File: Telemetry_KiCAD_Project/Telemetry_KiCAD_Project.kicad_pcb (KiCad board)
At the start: 4 copper layers, 80 x 87.3 mm, 67 parts, among them J1 50Ω SMA Connector, J2 DB37_Male, J3 10118192-0001LF, U2 Si4463, U3 ADL5521, U4 Si4463, U5 STM32L562VET, U6 LM317T, U7 USBLC6-2SC6, Y1 30MHz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

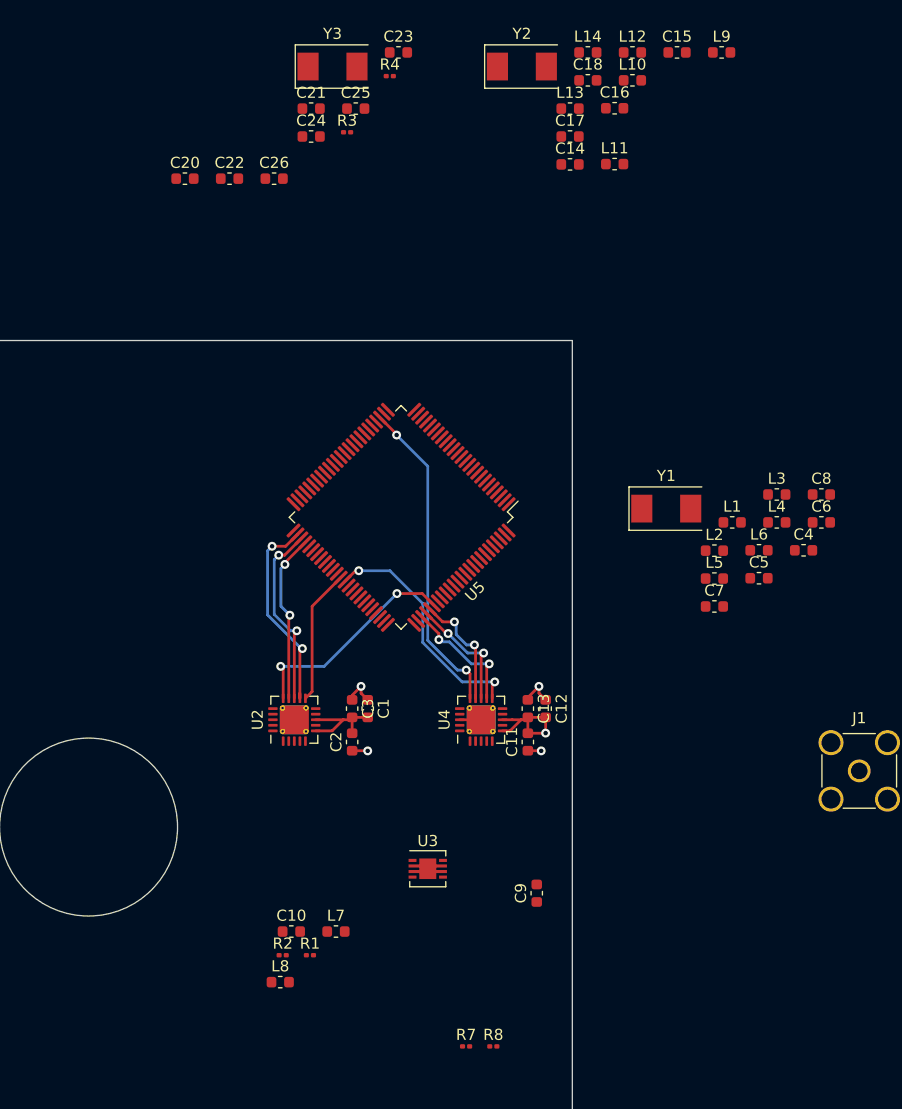
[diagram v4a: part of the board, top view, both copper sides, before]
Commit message: Added TX/RX matching network passives to PCB
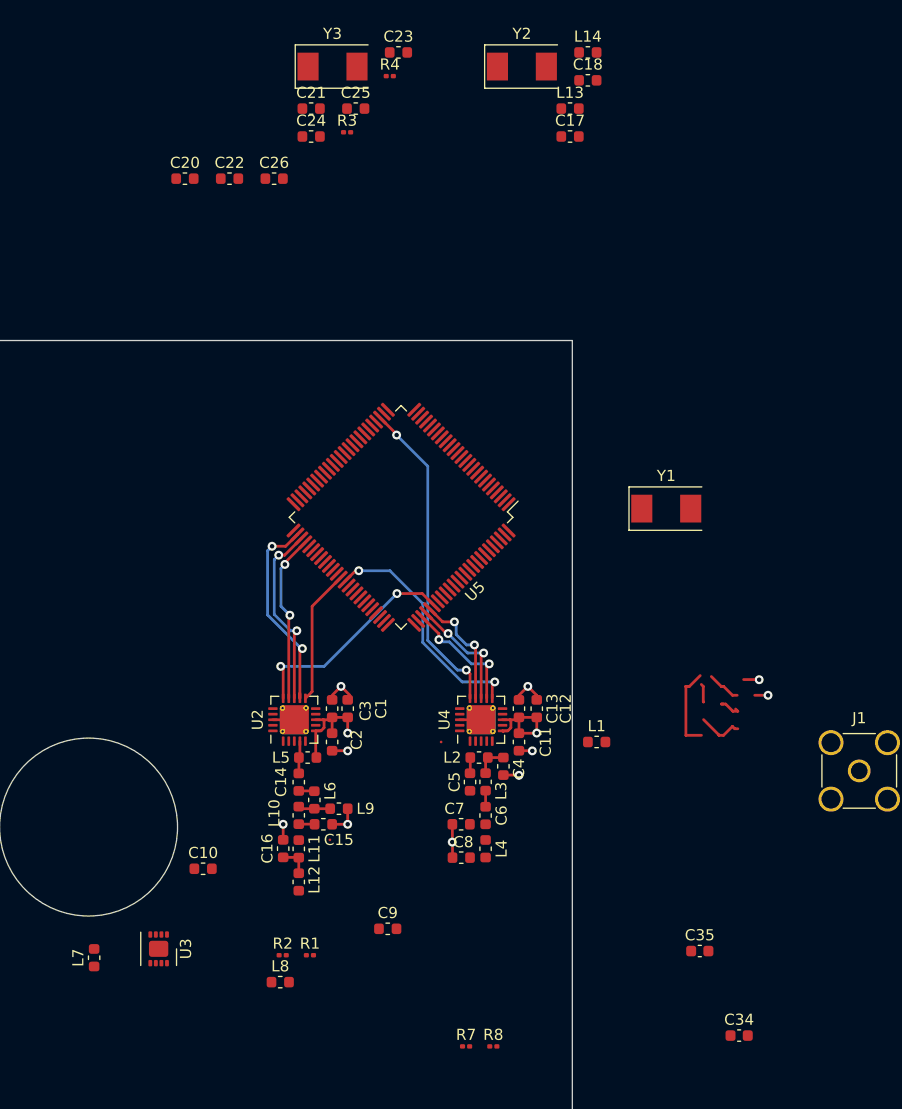
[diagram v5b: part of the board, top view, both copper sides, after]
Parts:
- added C34: C_Small, Capacitor_SMD:C_0603_1608Metric, F.Cu at (201.8, 117.8)
- added C35: C_Small, Capacitor_SMD:C_0603_1608Metric, F.Cu at (198.3, 110.2)
- C14: value C_Small -> 4.7pF
- C15, C16: value C_Small -> 3.3pF
- C4: value C_Small -> 3pF
- C5: value C_Small -> 1pF
- C6: value C_Small -> DC_Blocking
- C7, C8: value C_Small -> 4.3pF
- L1, L5: value L_Small -> 100nH
- L10, L12: value L_Small -> 11nH
- L11, L3: value L_Small -> 22nH
- L2: value L_Small -> 18nH
- L4: value L_Small -> 8.2nH
- L6: value L_Small -> 3.3nH
- L9: value L_Small -> 6.2nH
- U3: footprint Package_CSP:Analog_LFCSP-8-1EP_3x3mm_P0.5mm_EP1.53x1.85mm -> Package_CSP:LFCSP-8-1EP_3x3mm_P0.5mm_EP1.45x1.74mm
- moved L12 80.4 mm to (162.2, 104.0), turned to 270 degrees
- moved C15 76.3 mm to (164.4, 98.8)
- moved L9 76.2 mm to (165.8, 97.4)
- moved C16 72.9 mm to (160.8, 101.0), turned to 90 degrees
- moved L10 72.6 mm to (162.2, 98.0), turned to 270 degrees
- moved L11 67.8 mm to (162.2, 101.0), turned to 270 degrees
- moved C14 60.7 mm to (162.2, 95.0), turned to 270 degrees
- moved C8 46.0 mm to (176.8, 101.8), turned to 180 degrees
- moved L6 45.9 mm to (163.6, 96.6), turned to 270 degrees
- moved C6 40.1 mm to (179.0, 98.0), turned to 270 degrees
- moved L5 40.0 mm to (163.0, 92.8)
- moved L4 39.3 mm to (179.0, 101.0), turned to 270 degrees
- moved L3 36.8 mm to (179.0, 95.0), turned to 270 degrees
- moved C4 33.3 mm to (180.6, 93.6), turned to 90 degrees
- moved C5 31.8 mm to (177.6, 95.0), turned to 270 degrees
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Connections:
- C15 pad 2: Net-(C15-Pad2) -> GND
- C16 pad 1: GND -> Net-(C16-Pad1)
- C16 pad 2: Net-(C15-Pad1) -> GND
- C18 pad 2: /RX_Si4463/RF_Out -> Net-(C18-Pad2)
- C4 pad 1: Net-(C4-Pad1) -> GND
- C6 pad 1: GND -> Net-(C5-Pad2)
- C6 pad 2: Net-(C5-Pad1) -> Net-(C6-Pad2)
- C7 pad 1: GND -> Net-(C6-Pad2)
- C7 pad 2: Net-(C7-Pad2) -> GND
- C8 pad 1: GND -> /RX_Si4463/RF_Out
- C8 pad 2: /ADL_Amplifier/RF_In -> GND
- L1 pad 1: +3V3 -> Net-(L1-Pad1)
- L1 pad 2: Net-(C4-Pad2) -> +3V3
- L10 pad 2: Net-(C15-Pad2) -> Net-(C15-Pad1)
- L11 pad 1: Net-(C14-Pad1) -> Net-(C15-Pad1)
- L11 pad 2: Net-(C15-Pad1) -> Net-(C16-Pad1)
- L12 pad 1: Net-(L10-Pad1) -> Net-(C16-Pad1)
- L12 pad 2: Net-(C15-Pad1) -> /ADL_Amplifier/RF_In
- L14 pad 2: /RX_Si4463/RF_Out -> Net-(C18-Pad2)
- L2 pad 1: Net-(L2-Pad1) -> Net-(C5-Pad1)
- L2 pad 2: Net-(C5-Pad2) -> Net-(C4-Pad2)
- L3 pad 1: Net-(C4-Pad1) -> Net-(C4-Pad2)
- L3 pad 2: Net-(C5-Pad1) -> Net-(C5-Pad2)
- L4 pad 1: Net-(L2-Pad1) -> Net-(C6-Pad2)
- L4 pad 2: Net-(C5-Pad1) -> /RX_Si4463/RF_Out
- L5 pad 1: Net-(C5-Pad1) -> Net-(C14-Pad1)
- L5 pad 2: Net-(C7-Pad2) -> +3V3
- L6 pad 1: Net-(C7-Pad2) -> Net-(C14-Pad2)
- L6 pad 2: /ADL_Amplifier/RF_In -> Net-(L10-Pad1)
- L9 pad 1: +3V3 -> Net-(L10-Pad1)
- L9 pad 2: Net-(C14-Pad2) -> GND
- U2 pad 2: Net-(L2-Pad1) -> Net-(U2-Pad2)
- U2 pad 3: Net-(C5-Pad2) -> Net-(U2-Pad3)
- U2 pad 4: Net-(C4-Pad2) -> Net-(C14-Pad1)
- U4 pad 2: Net-(L10-Pad1) -> Net-(C5-Pad1)
- U4 pad 3: Net-(C15-Pad2) -> Net-(C4-Pad2)
- U4 pad 4: Net-(C14-Pad2) -> Net-(L1-Pad1)
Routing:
- net GND: track 12.8 -> 24.0 mm, vias 5 -> 10
- net Net-(C4-Pad2): track 0.00 -> 9.80 mm
- net Net-(C6-Pad2): track 0.00 -> 7.51 mm
- net /RX_Si4463/RF_Out: track 0.00 -> 4.12 mm
- net Net-(C14-Pad1): track 0.00 -> 2.94 mm
- net Net-(L10-Pad1): track 0.00 -> 2.90 mm
- net Net-(C16-Pad1): track 0.00 -> 2.81 mm
- net +3V3: track 21.4 -> 19.2 mm, vias 1 -> 2
- net Net-(C5-Pad2): track 0.00 -> 1.45 mm
- net Net-(C15-Pad1): track 0.00 -> 1.45 mm
- net Net-(C5-Pad1): track 0.00 -> 1.42 mm
- net Net-(C14-Pad2): track 0.00 -> 1.41 mm
- net Net-(L1-Pad1): track 0.00 -> 1.20 mm, vias 0 -> 1

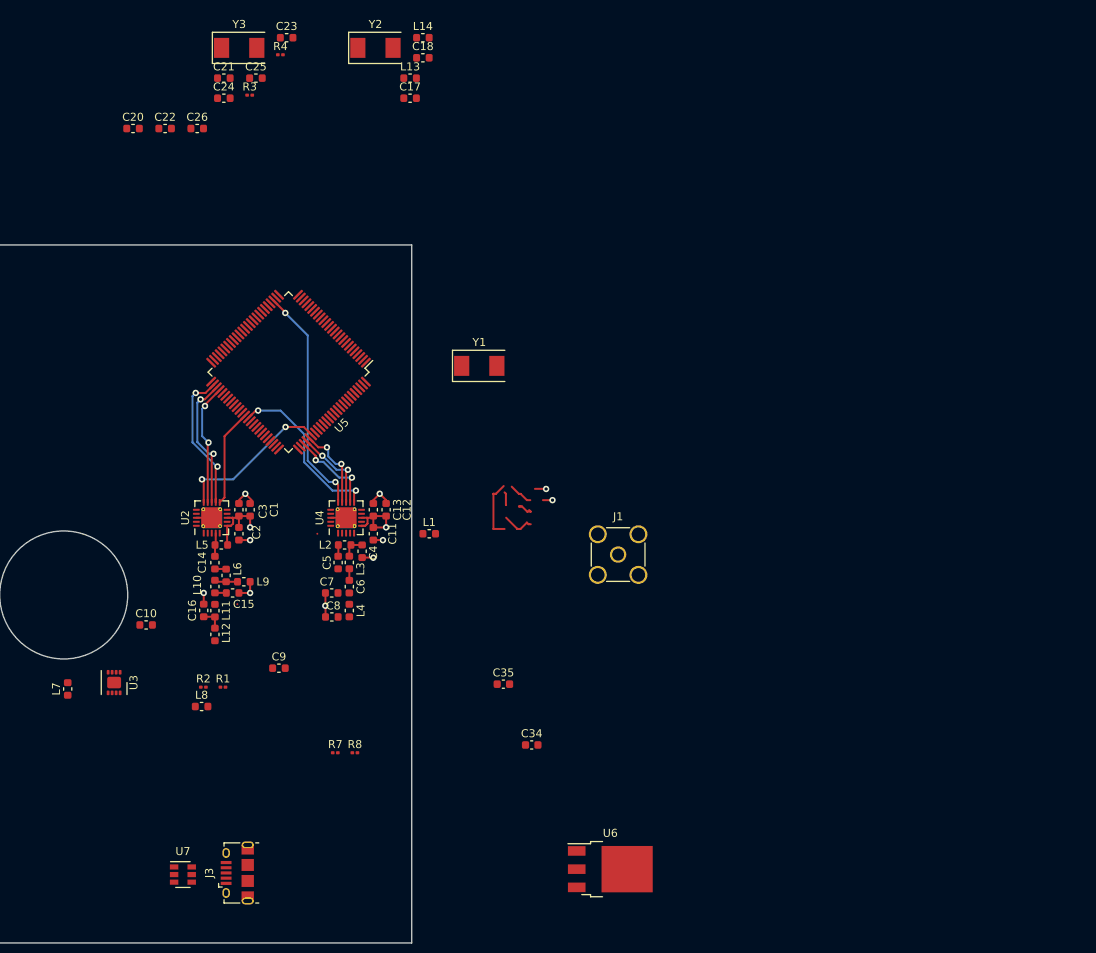
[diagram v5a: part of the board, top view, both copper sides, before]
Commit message: Added RSD Duplexer Footprint, rearranged RF matching networks
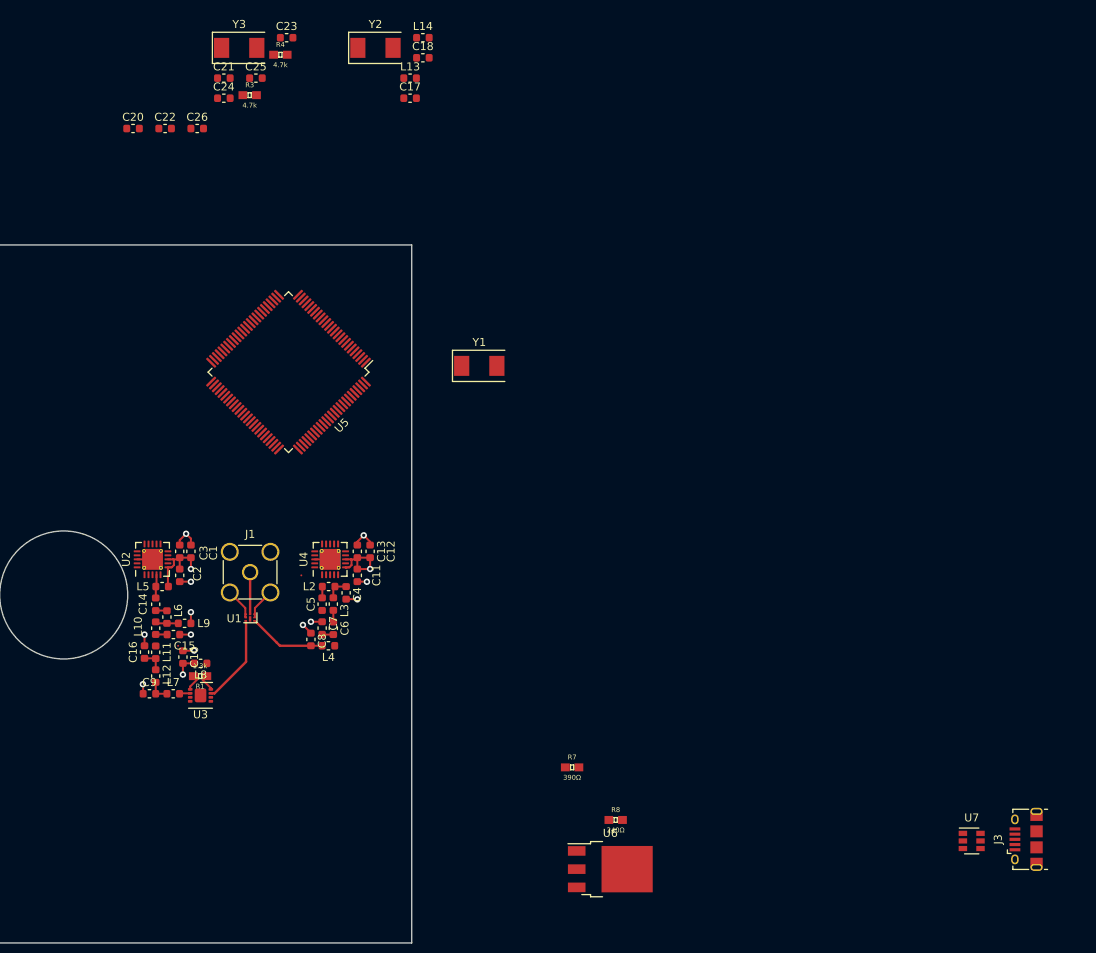
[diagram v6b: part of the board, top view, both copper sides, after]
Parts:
- removed C34, C35: C_Small, Capacitor_SMD:C_0603_1608Metric
- removed L1: 100nH, Inductor_SMD:L_0603_1608Metric
- removed R2: R_Small, Resistor_SMD:R_0201_0603Metric
- added U1: RSD-897.500-942.500-1612-TR, RDT_Custom_Footprints:RSD-897.500-942.500-1612-TR, F.Cu at (167.4, 102.5)
- L7: value L_Small -> 8.2nH
- R1, R3, R4, R7, R8: footprint Resistor_SMD:R_0201_0603Metric -> Resistors:0603
- moved J3 98.7 mm to (263.6, 129.6)
- moved U7 98.7 mm to (256.8, 129.8)
- moved J1 46.1 mm to (166.6, 96.2)
- moved R8 33.7 mm to (212.3, 127.2)
- moved R7 29.7 mm to (206.8, 120.6)
- moved C9 16.5 mm to (154.0, 111.4)
- moved L7 13.2 mm to (157.0, 111.4), turned to 0 degrees
- moved U3 10.9 mm to (160.4, 111.6), turned to 0 degrees
- moved C15 9.04 mm to (157.0, 104.0)
- moved C16 9.04 mm to (153.4, 106.2)
- moved L5 9.04 mm to (155.6, 98.0)
- moved L6 9.04 mm to (156.2, 101.8)
- moved C1 9.04 mm to (159.2, 93.6)
- moved L9 9.04 mm to (158.4, 102.6)
- moved U2 9.04 mm to (154.4, 94.6)
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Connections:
- C10 pad 2: Net-(C10-Pad2) -> +5V
- L8 pad 2: Net-(C10-Pad2) -> +5V
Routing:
- net /~RX_SEL: track 29.1 -> 0.00 mm, vias 2 -> 0
- net /~RX_IRQ: track 21.7 -> 0.00 mm, vias 2 -> 0
- net /~TX_SEL: track 19.9 -> 0.00 mm, vias 2 -> 0
- net /TX_SCL: track 18.5 -> 0.02 mm, vias 2 -> 0
- net /TX_SDO: track 17.0 -> 0.00 mm, vias 2 -> 0
- net /TX_SDI: track 15.3 -> 0.00 mm, vias 2 -> 0
- net /~TX_IRQ: track 12.2 -> 0.00 mm
- net /RX_SCL: track 11.3 -> 0.00 mm, vias 2 -> 0
- net /ADL_Amplifier/RF_Out: track 0.00 -> 10.9 mm
- net /RX_SDO: track 10.8 -> 0.00 mm, vias 2 -> 0
- net /RX_SDI: track 10.7 -> 0.00 mm, vias 2 -> 0
- net GND: track 24.0 -> 34.1 mm, vias 10 -> 13
- net Net-(C4-Pad2): track 9.80 -> 2.88 mm
- net Net-(C6-Pad2): track 7.51 -> 1.41 mm
- net /RX_Si4463/RF_Out: track 4.12 -> 9.52 mm
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
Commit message: PCB Layout Progress
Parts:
- removed C17, C18: C_Small, Capacitor_SMD:C_0603_1608Metric
- removed L13, L14: L_Small, Inductor_SMD:L_0603_1608Metric
- moved C19 183.4 mm to (124.0, 107.6), turned to 135 degrees
- moved C29 165.1 mm to (169.2, 127.3)
- moved C30 165.1 mm to (169.2, 129.8)
- moved C31 165.1 mm to (173.2, 127.3)
- moved C32 165.1 mm to (173.2, 129.8)
- moved C33 165.1 mm to (177.2, 127.3)
- moved R4 93.9 mm to (123.6, 113.0), turned to 90 degrees
- moved R3 90.5 mm to (123.6, 116.2), turned to 270 degrees
- moved C21 88.3 mm to (160.8, 122.8), turned to 315 degrees
- moved Y3 88.1 mm to (160.4, 118.6), turned to 315 degrees
- moved C22 82.3 mm to (165.4, 122.6), turned to 315 degrees
- moved C20 77.8 mm to (156.2, 118.4), turned to 135 degrees
- moved C26 77.2 mm to (179.6, 115.4), turned to 45 degrees
- moved C24 74.1 mm to (157.0, 110.8), turned to 225 degrees
- moved C23 71.9 mm to (172.4, 101.2), turned to 315 degrees
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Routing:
- net /MCU_L562VE/ABORT_1: track 0.00 -> 60.2 mm, vias 0 -> 2
- net /MCU_L562VE/ABORT_2: track 0.00 -> 57.5 mm, vias 0 -> 2
- net /MCU_L562VE/SPI1_SCK: track 0.00 -> 57.3 mm, vias 0 -> 2
- net /MCU_L562VE/SPI1_MOSI: track 0.00 -> 56.9 mm, vias 0 -> 2
- net /MCU_L562VE/SPI1_MISO: track 0.00 -> 54.7 mm, vias 0 -> 2
- net +5V: track 2.83 -> 56.9 mm
- net /37_Pin_DSUB_Bus/Alert_sda: track 0.00 -> 50.9 mm, vias 0 -> 2
- net /37_Pin_DSUB_Bus/Alert_scl: track 0.00 -> 49.4 mm, vias 0 -> 2
- net /~RX_IRQ: track 0.00 -> 44.7 mm, vias 0 -> 2
- net /TX_SCL: track 0.02 -> 35.4 mm, vias 0 -> 2
- net /TX_SDO: track 0.00 -> 35.1 mm, vias 0 -> 2
- net /TX_SDI: track 0.00 -> 35.0 mm, vias 0 -> 2
- net /RX_SCL: track 0.00 -> 33.2 mm, vias 0 -> 2
- net /RX_SDO: track 0.00 -> 32.9 mm, vias 0 -> 2
- net /RX_SDI: track 0.00 -> 32.5 mm, vias 0 -> 2
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
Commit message: PCB Layout Progress
Everything appears to be connected...
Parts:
- moved C28 215.3 mm to (168.8, 88.2), turned to 90 degrees
- moved D1 211.5 mm to (176.7, 94.6)
- moved FB1 206.2 mm to (179.6, 94.4)
- moved C27 200.0 mm to (180.0, 85.8)
- moved J3 88.5 mm to (183.9, 91.2)
- moved U7 87.6 mm to (178.0, 91.6)
- moved U6 66.7 mm to (161.8, 88.9), turned to 180 degrees
- moved R8 57.0 mm to (166.2, 93.6), turned to 180 degrees
- moved R7 47.3 mm to (169.8, 91.2)
- moved C31 20.7 mm to (155.9, 116.1), turned to 135 degrees
- moved C33 17.9 mm to (180.1, 109.7), turned to 45 degrees
- moved C29 17.2 mm to (157.1, 115.1), turned to 135 degrees
- moved C22 11.2 mm to (158.2, 114.0), turned to 135 degrees
- moved C30 9.82 mm to (165.1, 120.9), turned to 315 degrees
- moved C32 7.93 mm to (170.7, 122.3), turned to 225 degrees
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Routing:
- net +5V: track 56.9 -> 164.3 mm, vias 1 -> 5
- net /MCU_L562VE/DEBUG_SWDIO: track 0.00 -> 60.0 mm, vias 0 -> 2
- net /~RX_SEL: track 0.00 -> 55.8 mm, vias 0 -> 2
- net /37_Pin_DSUB_Bus/NRST: track 7.90 -> 57.6 mm, vias 0 -> 2
- net /37_Pin_DSUB_Bus/Alert_Active: track 0.00 -> 48.9 mm, vias 0 -> 1
- net /MCU_L562VE/DEBUG_SWCLK: track 4.60 -> 52.1 mm
- net +3V3: track 29.7 -> 73.7 mm, vias 6 -> 15
- net GND: track 46.6 -> 71.3 mm, vias 22 -> 37
- net /USB Connector and ESD/D+: track 0.00 -> 18.8 mm
- net /USB Connector and ESD/D-: track 0.00 -> 18.5 mm
- net (no net): track 0.00 -> 6.23 mm
- net Net-(R7-Pad1): track 0.00 -> 5.53 mm
- net /MCU_L562VE/ABORT_2: track 57.5 -> 61.7 mm
- net /MCU_L562VE/ABORT_1: track 60.2 -> 64.0 mm
- net /USB Connector and ESD/USB_CONN_D-: track 0.00 -> 3.69 mm
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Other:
- net class Default: clearance 0.2 -> 0.05
- rule trace_clearance: 0.2 -> 0.05
